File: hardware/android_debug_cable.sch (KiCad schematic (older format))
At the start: 12 parts, among them P1 USB_A, P2 CONN_01X04, P3 SJ-43514-SMT-TR, U1 TPS71718DCKR, U2 CP2103-GM

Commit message: Add v0.2_copperhead
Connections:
- net RX: now also P3.3 (P3); no longer P3.2 (P2)
- net TX: now also P3.2 (P2); no longer P3.3 (P3)
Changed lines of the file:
@@
 Wire Wire Line
 	3300 3050 3300 3250
-Wire Wire Line
-	3300 3150 3350 3150
 Text GLabel 2900 4900 2    60   Input ~ 0
 VCC
@@
 	1    0    0    -1
 $EndComp
+Text GLabel 7500 4200 0    60   Input ~ 0
+RX
 Text GLabel 7500 4100 0    60   Input ~ 0
-RX
-Text GLabel 7500 4200 0    60   Input ~ 0
 TX
 Text GLabel 7500 4300 0    60   Input ~ 0
@@
 	1    0    0    -1
 $EndComp
+Wire Wire Line
+	3300 3150 3350 3150
 $EndSCHEMATC

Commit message: Add first version of v0.4
Signed-off-by: Robert Foss <robert.foss@collabora.com>
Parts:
- removed C6: 0.1uF, Capacitors_SMD:C_0402, symbol C_Small
- removed P1: USB_A, connectors:usb-PCB, symbol USB_A
- removed U2: CP2103-GM, Housings_DFN_QFN:QFN-28-1EP_5x5mm_Pitch0.5mm, symbol cp2103
- added P1: USB_OTG, Connectors:USB_Micro-B, symbol USB_OTG
- added U2: CP2102N-A01-GQFN24, Housings_DFN_QFN:QFN-24-1EP_4x4mm_Pitch0.5mm, symbol CP2102N-A01-GQFN24
- C1: value 0.1uF -> 1uF
- P2: renamed from P3; value SJ-43514-SMT-TR -> 50-00397; footprint 3-5mm_4pole_jack:3.5mm_4pin_jack -> 50-00397:50-00397
- R1: value 10k -> 1k
- U1: value TPS71718DCKR -> TCR2EF18; footprint TO_SOT_Packages_SMD:SC-70-5 -> TO_SOT_Packages_SMD:SOT-23-5
- renumbered C4 to C3, C5 to C4, P2 to P3
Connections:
- net GND: now also P1.5 (GND), P1.6 (Shield), U2.2 (GND), U2.25 (GND); no longer C1.1, C2.1
- net RX: now also U2.21 (TXD)
- net TX: now also U2.20 (RXD)
- net USB_D+: now also P1.3 (D+), U2.3 (D+)
- net USB_D-: now also P1.2 (D-), U2.4 (D-)
- net V1.8: now also R1.2, U2.5 (VIO)
- net VCC: now also P1.1 (VBUS), U2.8 (VBUS); no longer R1.1
- new net: C1.1, U2.6 (VDD)
- new net: C2.1, U2.7 (REGIN)
- new net: R1.1, U2.9 (~RSTb)
- no-connect marks 1 -> 0
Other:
- moved on the sheet: C1, C2, C3, C4, U1, W1

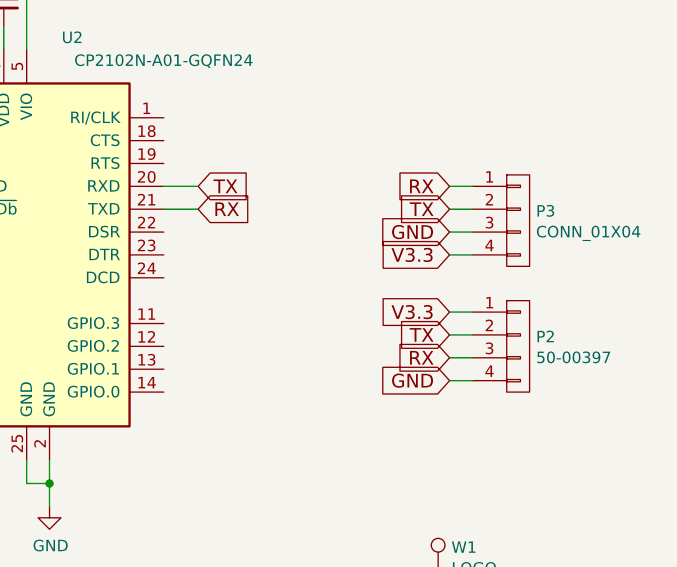
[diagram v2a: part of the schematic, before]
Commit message: Changed 3.5mm connector pinout
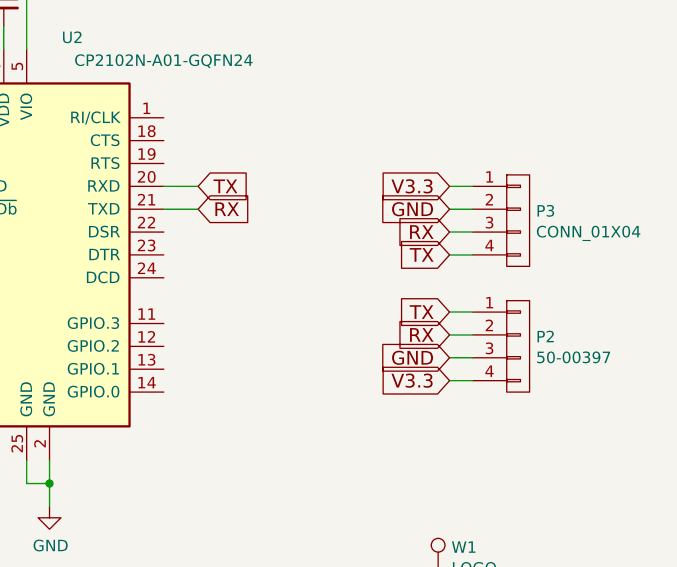
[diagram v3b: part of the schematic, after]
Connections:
- net GND: now also P2.3 (P3), P3.2 (P2); no longer P2.4 (P4), P3.3 (P3)
- net RX: now also P2.2 (P2), P3.3 (P3); no longer P2.3 (P3), P3.1 (P1)
- net TX: now also P2.1 (P1), P3.4 (P4); no longer P2.2 (P2), P3.2 (P2)
- net V3.3: now also P2.4 (P4), P3.1 (P1); no longer P2.1 (P1), P3.4 (P4)
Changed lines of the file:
@@
 	1    0    0    -1
 $EndComp
-Text GLabel 7500 3750 0    60   Input ~ 0
+Text GLabel 7500 3450 0    60   Input ~ 0
 V3.3
 Wire Wire Line
 	7500 3750 7600 3750
-Text GLabel 7500 3650 0    60   Input ~ 0
+Text GLabel 7500 3550 0    60   Input ~ 0
 GND
 Wire Wire Line
 	7500 3650 7600 3650
-Text GLabel 7500 3550 0    60   Input ~ 0
+Text GLabel 7500 3750 0    60   Input ~ 0
 TX
 Wire Wire Line
 	7500 3550 7600 3550
-Text GLabel 7500 3450 0    60   Input ~ 0
+Text GLabel 7500 3650 0    60   Input ~ 0
 RX
 Wire Wire Line
@@
 	1    0    0    -1
 $EndComp
+Text GLabel 7500 4100 0    60   Input ~ 0
+RX
+Text GLabel 7500 4000 0    60   Input ~ 0
+TX
 Text GLabel 7500 4200 0    60   Input ~ 0
-RX
-Text GLabel 7500 4100 0    60   Input ~ 0
-TX
+GND
 Text GLabel 7500 4300 0    60   Input ~ 0
-GND
-Text GLabel 7500 4000 0    60   Input ~ 0
 V3.3
 Wire Wire Line

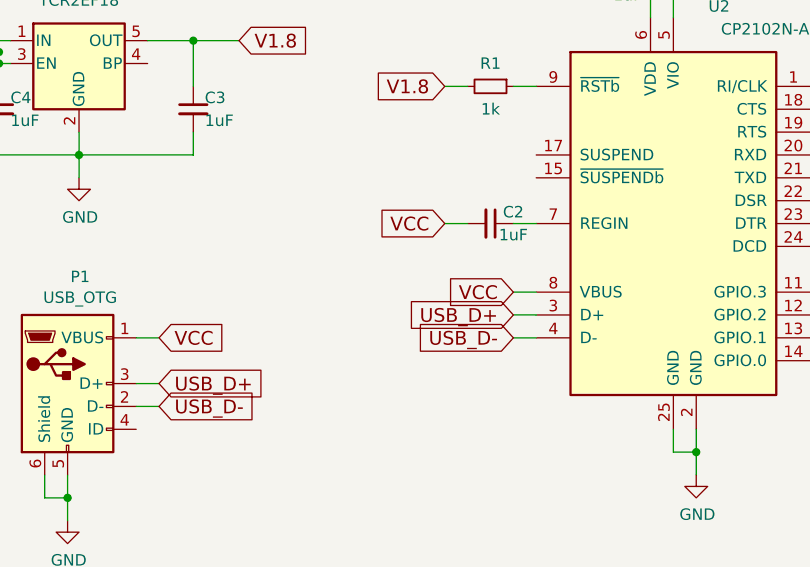
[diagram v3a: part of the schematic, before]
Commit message: Fixed CP2102N power sourcing
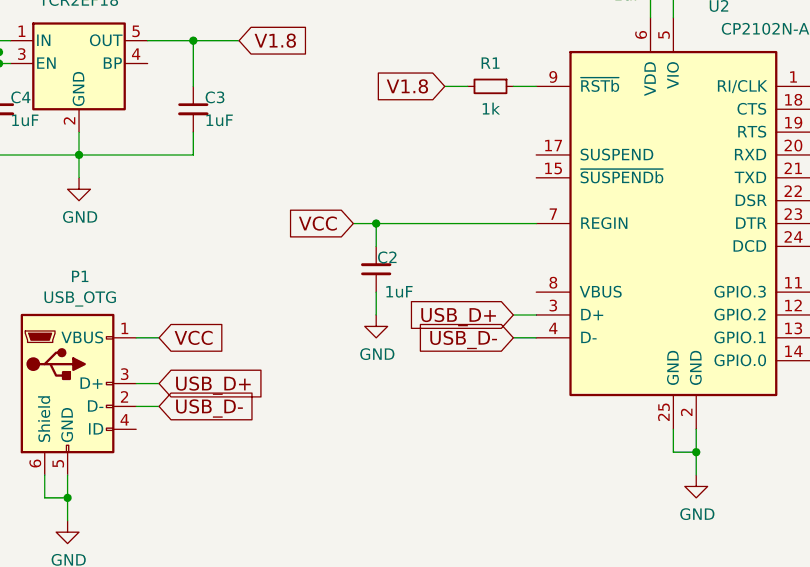
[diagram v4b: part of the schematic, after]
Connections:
- net GND: now also C2.1
- net VCC: now also U2.7 (REGIN); no longer U2.8 (VBUS)
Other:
- moved on the sheet: C2
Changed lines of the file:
@@
 	1    0    0    -1
 $EndComp
-Wire Wire Line
-	2750 2950 2700 2950
-Wire Wire Line
-	2700 2950 2700 3150
 Text GLabel 3400 4250 2    60   Input ~ 0
 VCC
 Text GLabel 2600 3000 0    60   Input ~ 0
 VCC
-Wire Wire Line
-	2600 3000 2700 3000
-Connection ~ 2700 3000
 $Comp
 L C_Small C4
@@
 	1    0    0    -1
 $EndComp
-Connection ~ 2700 3050
 $Comp
 L GND #PWR02
@@
 	1    0    0    -1
 $EndComp
-Connection ~ 3050 3450
-Wire Wire Line
-	3350 2950 3750 2950
-Wire Wire Line
-	3550 2950 3550 3150
 Text GLabel 3750 2950 2    60   Input ~ 0
 V1.8
-Connection ~ 3550 2950
 Text GLabel 3400 4450 2    60   Input ~ 0
 USB_D+
@@
 Text GLabel 4950 4250 0    60   Input ~ 0
 USB_D-
-Wire Wire Line
-	5050 4150 4950 4150
-Wire Wire Line
-	4950 4250 5050 4250
-Text GLabel 4950 4050 0    60   Input ~ 0
-VCC
-Wire Wire Line
-	4950 4050 5050 4050
 Text GLabel 4650 3150 0    60   Input ~ 0
 V1.8
@@
 L C_Small C2
 U 1 1 57AE72EC
-P 4850 3750
-F 0 "C2" V 4800 3850 50  0000 C CNN
-F 1 "1uF" V 4900 3850 50  0000 C CNN
-F 2 "Capacitors_SMD:C_0402" H 4850 3750 50  0001 C CNN
-F 3 "" H 4850 3750 50  0000 C CNN
-	1    4850 3750
-	0    1    1    0
+P 4350 3950
+F 0 "C2" H 4300 3900 50  0000 C CNN
+F 1 "1uF" H 4250 4050 50  0000 C CNN
+F 2 "Capacitors_SMD:C_0402" H 4350 3950 50  0001 C CNN
+F 3 "" H 4350 3950 50  0000 C CNN
+	1    4350 3950
+	-1   0    0    1
 $EndComp
 Text GLabel 5550 2450 1    60   Output ~ 0
 V3.3
-Text GLabel 4650 3750 0    60   Input ~ 0
+Text GLabel 4250 3750 0    60   Input ~ 0
 VCC
 Text GLabel 6400 3450 2    60   Input ~ 0
 TX
-Wire Wire Line
-	6400 3450 6250 3450
 Text GLabel 6400 3550 2    60   Input ~ 0
 RX
-Wire Wire Line
-	6400 3550 6250 3550
 $Comp
 L CONN_01X04 P3
@@
 Text GLabel 7500 3450 0    60   Input ~ 0
 V3.3
-Wire Wire Line
-	7500 3750 7600 3750
 Text GLabel 7500 3550 0    60   Input ~ 0
 GND
-Wire Wire Line
-	7500 3650 7600 3650
 Text GLabel 7500 3750 0    60   Input ~ 0
 TX
-Wire Wire Line
-	7500 3550 7600 3550
 Text GLabel 7500 3650 0    60   Input ~ 0
 RX
-Wire Wire Line
-	7500 3450 7600 3450
 $Comp
 L CONN_01X04 P2
@@
 Text GLabel 7500 4300 0    60   Input ~ 0
 V3.3
-Wire Wire Line
-	7500 4300 7600 4300
-Wire Wire Line
-	7600 4200 7500 4200
-Wire Wire Line
-	7500 4100 7600 4100
-Wire Wire Line
-	7600 4000 7500 4000
 $Comp
 L TEST_1P W1
@@
 	1    0    0    -1
 $EndComp
-Wire Wire Line
-	2700 3050 2750 3050
-Wire Wire Line
-	2700 3450 2700 3350
-Wire Wire Line
-	3050 3350 3050 3550
-Wire Wire Line
-	3550 3450 3550 3350
-Wire Wire Line
-	2700 3450 3550 3450
 $Comp
 L CP2102N-A01-GQFN24 U2
@@
 	1    0    0    -1
 $EndComp
-Wire Wire Line
-	5750 4650 5750 4850
-Wire Wire Line
-	5650 4650 5650 4750
-Wire Wire Line
-	5650 4750 5750 4750
-Connection ~ 5750 4750
-Wire Wire Line
-	5050 3750 4950 3750
-Wire Wire Line
-	4650 3750 4750 3750
-Wire Wire Line
-	5550 2750 5550 2850
-Wire Wire Line
-	5550 2550 5550 2450
 $Comp
 L R_Small R1
@@
 	0    1    1    0
 $EndComp
-Wire Wire Line
-	5050 3150 4950 3150
-Wire Wire Line
-	4650 3150 4750 3150
 Text GLabel 5650 2450 1    60   Input ~ 0
 V1.8
@@
 	1    0    0    -1
 $EndComp
+$Comp
+L GND #PWR?
+U 1 1 59497964
+P 4350 4150
+F 0 "#PWR?" H 4350 3900 50  0001 C CNN
+F 1 "GND" H 4355 3977 50  0000 C CNN
+F 2 "" H 4350 4150 50  0001 C CNN
+F 3 "" H 4350 4150 50  0001 C CNN
+	1    4350 4150
+	1    0    0    -1
+$EndComp
+Wire Wire Line
+	2750 2950 2700 2950
+Wire Wire Line
+	2700 2950 2700 3150
+Wire Wire Line
+	2600 3000 2700 3000
+Connection ~ 2700 3000
+Connection ~ 2700 3050
+Connection ~ 3050 3450
+Wire Wire Line
+	3350 2950 3750 2950
+Wire Wire Line
+	3550 2950 3550 3150
+Connection ~ 3550 2950
+Wire Wire Line
+	5050 4150 4950 4150
+Wire Wire Line
+	4950 4250 5050 4250
+Wire Wire Line
+	6400 3450 6250 3450
+Wire Wire Line
+	6400 3550 6250 3550
+Wire Wire Line
+	7500 3750 7600 3750
+Wire Wire Line
+	7500 3650 7600 3650
+Wire Wire Line
+	7500 3550 7600 3550
+Wire Wire Line
+	7500 3450 7600 3450
+Wire Wire Line
+	7500 4300 7600 4300
+Wire Wire Line
+	7600 4200 7500 4200
+Wire Wire Line
+	7500 4100 7600 4100
+Wire Wire Line
+	7600 4000 7500 4000
+Wire Wire Line
+	2700 3050 2750 3050
+Wire Wire Line
+	2700 3450 2700 3350
+Wire Wire Line
+	3050 3350 3050 3550
+Wire Wire Line
+	3550 3450 3550 3350
+Wire Wire Line
+	2700 3450 3550 3450
+Wire Wire Line
+	5750 4650 5750 4850
+Wire Wire Line
+	5650 4650 5650 4750
+Wire Wire Line
+	5650 4750 5750 4750
+Connection ~ 5750 4750
+Wire Wire Line
+	4250 3750 5050 3750
+Wire Wire Line
+	5550 2750 5550 2850
+Wire Wire Line
+	5550 2550 5550 2450
+Wire Wire Line
+	5050 3150 4950 3150
+Wire Wire Line
+	4650 3150 4750 3150
 Wire Wire Line
 	2900 4850 2900 4950
@@
 Wire Wire Line
 	5650 2450 5650 2850
+Connection ~ 4350 3750
+Wire Wire Line
+	4350 4150 4350 4050
+Wire Wire Line
+	4350 3850 4350 3750
 $EndSCHEMATC

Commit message: Edit MicoUSB footprint
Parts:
- P1: footprint Connectors:USB_Micro-B -> usb_otg:USB_Micro-B
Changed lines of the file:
@@
 F 0 "P1" H 3055 4917 50  0000 C CNN
 F 1 "USB_OTG" H 3055 4826 50  0000 C CNN
-F 2 "Connectors:USB_Micro-B" H 3150 4400 50  0001 C CNN
+F 2 "usb_otg:USB_Micro-B" H 3150 4400 50  0001 C CNN
 F 3 "" H 3150 4400 50  0001 C CNN
 	1    3000 4450
@@
 $EndComp
 $Comp
-L GND #PWR?
+L GND #PWR04
 U 1 1 59497964
 P 4350 4150
-F 0 "#PWR?" H 4350 3900 50  0001 C CNN
+F 0 "#PWR04" H 4350 3900 50  0001 C CNN
 F 1 "GND" H 4355 3977 50  0000 C CNN
 F 2 "" H 4350 4150 50  0001 C CNN

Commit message: v0.6
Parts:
- C1: footprint Capacitors_SMD:C_0402 -> (none)
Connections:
- net GND: now also C1.2
- net V3.3: now also C1.1, U2.6 (VDD); no longer C1.2
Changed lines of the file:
@@
 V1.8
-$Comp
-L C_Small C1
-U 1 1 57AE72A2
-P 5550 2650
-F 0 "C1" H 5650 2600 50  0000 C CNN
-F 1 "1uF" H 5650 2750 50  0000 C CNN
-F 2 "Capacitors_SMD:C_0402" H 5550 2650 50  0001 C CNN
-F 3 "" H 5550 2650 50  0000 C CNN
-	1    5550 2650
-	-1   0    0    1
-$EndComp
 $Comp
 L C_Small C2
@@
 	4250 3750 5050 3750
 Wire Wire Line
-	5550 2750 5550 2850
-Wire Wire Line
-	5550 2550 5550 2450
+	5550 2450 5550 2850
 Wire Wire Line
 	5050 3150 4950 3150
@@
 Wire Wire Line
 	4350 3850 4350 3750
+$Comp
+L C_Small C1
+U 1 1 59579678
+P 5350 2650
+F 0 "C1" V 5250 2700 50  0000 C CNN
+F 1 "1uF" V 5450 2700 50  0000 C CNN
+F 2 "" H 5350 2650 50  0001 C CNN
+F 3 "" H 5350 2650 50  0001 C CNN
+	1    5350 2650
+	0    1    1    0
+$EndComp
+Wire Wire Line
+	5450 2650 5550 2650
+Connection ~ 5550 2650
+$Comp
+L GND #PWR?
+U 1 1 595798C6
+P 5150 2750
+F 0 "#PWR?" H 5150 2500 50  0001 C CNN
+F 1 "GND" H 5155 2577 50  0000 C CNN
+F 2 "" H 5150 2750 50  0001 C CNN
+F 3 "" H 5150 2750 50  0001 C CNN
+	1    5150 2750
+	1    0    0    -1
+$EndComp
+Wire Wire Line
+	5150 2750 5150 2650
+Wire Wire Line
+	5150 2650 5250 2650
 $EndSCHEMATC

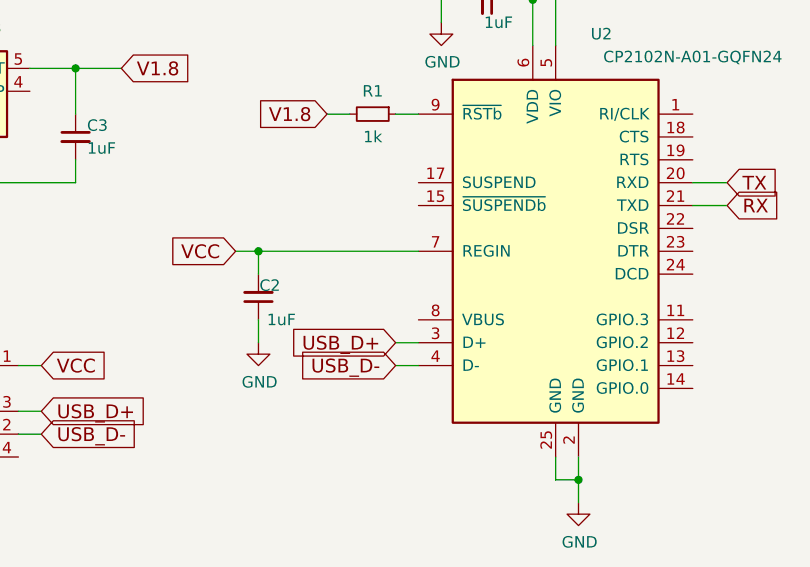
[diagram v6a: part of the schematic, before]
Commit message: Fixed VBUS not being connected, shrunk connector through holes
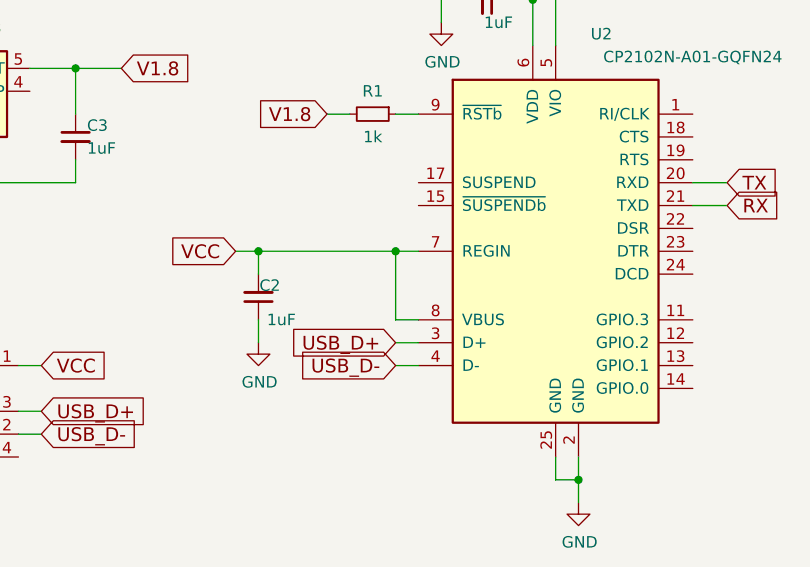
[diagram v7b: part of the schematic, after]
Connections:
- net VCC: now also U2.8 (VBUS)
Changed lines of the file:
@@
 Wire Wire Line
 	5150 2650 5250 2650
+Wire Wire Line
+	5050 4050 4950 4050
+Wire Wire Line
+	4950 4050 4950 3750
+Connection ~ 4950 3750
 $EndSCHEMATC
